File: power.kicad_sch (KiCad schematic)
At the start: 25 parts, among them J15 Screw_Terminal_01x04, U4 TPS5604, U5 TPS5604

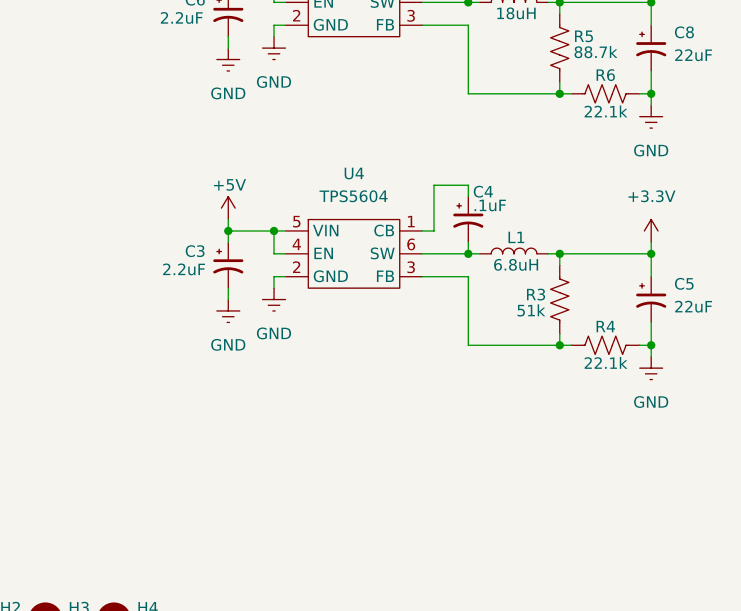
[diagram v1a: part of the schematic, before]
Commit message: mostly routed
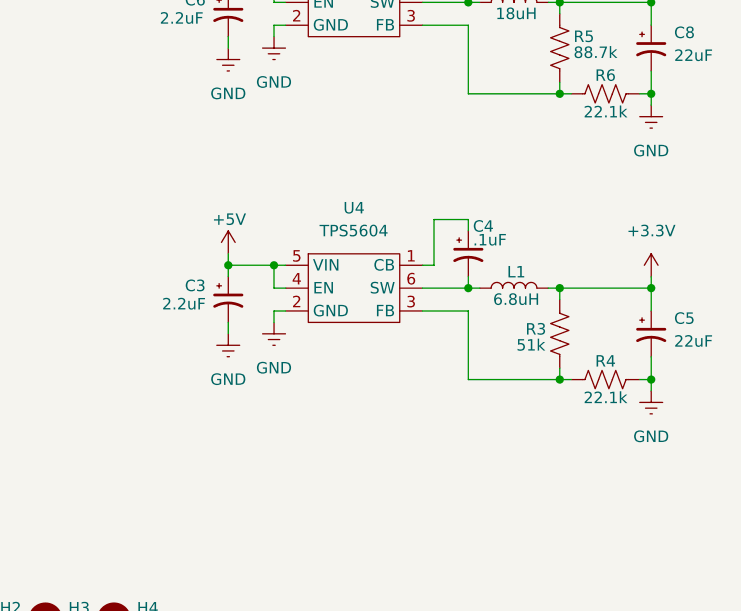
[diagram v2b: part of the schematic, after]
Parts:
- C8: footprint Capacitor_SMD:C_0805_2012Metric_Pad1.18x1.45mm_HandSolder -> Capacitor_SMD:C_0603_1608Metric_Pad1.08x0.95mm_HandSolder
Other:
- moved on the sheet: C3, C4, C5, L1, R3, R4, U4

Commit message: Rev A: release to fab (JLCPCB, 5 PCB / 2 assembled)
Board
- Outline set to exactly 160 x 100 mm; plane zones resized to match
- UART brought out on J20 (1x6 SMD, FTDI pinout) with series
  resistors R98/R99 and TVS D48
- J1 and J20 changed to SMD headers (C52016780, C41417363)
- L1/L2 moved to Sunlord SWPA4030S footprints; regulator tracks rerouted
- 41 test points added (35 top, 6 bottom), including SPI access
- Crystal case pins (Y1/Y2 pads 2, 4) tied to GND
- SW2 changed to 2-pin push button symbol
- R84-R91 changed from 2.2k to 10k to cut dissipation at 24 V
- Thermal vias in U1/U14 enlarged to 0.3 mm drill; 27 +24V vias added
  under U8-U11; solid plane connections on high-current pins
- Input/output rows and edge connectors aligned
- /inputs/_SG4 track and via moved clear of R74 pad 1

Schematic
- ERC cleared: no-connects, PWR_FLAGs, pin types, off-grid items
- Symbols moved to project library robust-io
- Test point symbols added on processor and power sheets

Rules
- Custom DRC rule for U7 pad-to-pad clearance (0.15 mm)
- Minimum through hole 0.2 mm; silk-to-edge check ignored

Fab outputs (fab/)
- make_gerbers.sh: Gerbers, drill and position export via kicad-cli
- JLC BOM with LCSC part numbers on all 50 SMD lines
- JLC placement file with per-part rotation offsets
  (cpl_rotation_offsets.json), verified in JLC placement preview
- Through-hole BOM and test point list

DRC: 4 library-mismatch warnings (J20, U1, U14, U7), 0 errors
ERC: clean
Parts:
- added TP1: +3.3V, TestPoint:TestPoint_Pad_D1.0mm, symbol Connector:TestPoint
- added TP14: ISENSE, TestPoint:TestPoint_Pad_D1.0mm, symbol Connector:TestPoint
- added TP15: ISENSE_PROT, TestPoint:TestPoint_Pad_D1.0mm, symbol Connector:TestPoint
- added TP16: AMUX0, TestPoint:TestPoint_Pad_D1.0mm, symbol Connector:TestPoint
- added TP17: IPROPIM0, TestPoint:TestPoint_Pad_D1.0mm, symbol Connector:TestPoint
- added TP18: IPROPIM1, TestPoint:TestPoint_Pad_D1.0mm, symbol Connector:TestPoint
- added TP19: DSELn, TestPoint:TestPoint_Pad_D1.0mm, symbol Connector:TestPoint
- added TP2: +5V, TestPoint:TestPoint_Pad_D1.0mm, symbol Connector:TestPoint
- added TP20: DEN0, TestPoint:TestPoint_Pad_D1.0mm, symbol Connector:TestPoint
- added TP21: DEN1, TestPoint:TestPoint_Pad_D1.0mm, symbol Connector:TestPoint
- added TP22: DEN2, TestPoint:TestPoint_Pad_D1.0mm, symbol Connector:TestPoint
- added TP23: DEN3, TestPoint:TestPoint_Pad_D1.0mm, symbol Connector:TestPoint
- added TP24: EN_M0, TestPoint:TestPoint_Pad_D1.0mm, symbol Connector:TestPoint
- added TP25: EN_M1, TestPoint:TestPoint_Pad_D1.0mm, symbol Connector:TestPoint
- added TP26: PH_M0, TestPoint:TestPoint_Pad_D1.0mm, symbol Connector:TestPoint
- added TP27: PH_M1, TestPoint:TestPoint_Pad_D1.0mm, symbol Connector:TestPoint
- added TP28: nSLEEPMn, TestPoint:TestPoint_Pad_D1.0mm, symbol Connector:TestPoint
- added TP29: FAULTMn, TestPoint:TestPoint_Pad_D1.0mm, symbol Connector:TestPoint
- added TP3: +24V, TestPoint:TestPoint_Pad_D1.0mm, symbol Connector:TestPoint
- added TP30: DRV_OUT0, TestPoint:TestPoint_Pad_D1.0mm, symbol Connector:TestPoint
- added TP31: DRV_OUT1, TestPoint:TestPoint_Pad_D1.0mm, symbol Connector:TestPoint
- added TP32: DRV_OUT2, TestPoint:TestPoint_Pad_D1.0mm, symbol Connector:TestPoint
- added TP33: DRV_OUT3, TestPoint:TestPoint_Pad_D1.0mm, symbol Connector:TestPoint
- added TP34: DRV_OUT4, TestPoint:TestPoint_Pad_D1.0mm, symbol Connector:TestPoint
- added TP35: DRV_OUT5, TestPoint:TestPoint_Pad_D1.0mm, symbol Connector:TestPoint
- added TP36: DRV_OUT6, TestPoint:TestPoint_Pad_D1.0mm, symbol Connector:TestPoint
- added TP37: DRV_OUT7, TestPoint:TestPoint_Pad_D1.0mm, symbol Connector:TestPoint
- added TP38, TP39, TP40, TP41: GND, TestPoint:TestPoint_Pad_D1.0mm, symbol Connector:TestPoint
- added TP4: SCLK0, TestPoint:TestPoint_Pad_D1.0mm, symbol Connector:TestPoint
- added TP5: MOSI0, TestPoint:TestPoint_Pad_D1.0mm, symbol Connector:TestPoint
- added TP6: MISO0, TestPoint:TestPoint_Pad_D1.0mm, symbol Connector:TestPoint
- added TP7: CS_IN0, TestPoint:TestPoint_Pad_D1.0mm, symbol Connector:TestPoint
- added TP9: INT_B0, TestPoint:TestPoint_Pad_D1.0mm, symbol Connector:TestPoint
- C44, C45: value 100uF -> 100uF 50V; footprint Capacitor_SMD:C_0805_2012Metric_Pad1.18x1.45mm_HandSolder -> Capacitor_SMD:CP_Elec_8x10
- C46: value 2.2uF -> 2.2uF 50V
- C47: value .1uF -> .1uF 50V
- D6: value SMCJ28A -> SMDJ24A
- L1: footprint Inductor_SMD:L_0805_2012Metric_Pad1.05x1.20mm_HandSolder -> Inductor_SMD:L_Sunlord_SWPA4030S
- L2: footprint Inductor_SMD:L_0805_2012Metric -> Inductor_SMD:L_Sunlord_SWPA4030S
- U4, U5: symbol rml_kicad_lib:TPS5604 -> robust-io:TPS5604
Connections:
- net +24V: now also TP3.1
- net +3.3V: now also TP1.1
- net +5V: now also TP2.1
- net GND: now also TP38.1, TP39.1, TP40.1, TP41.1
- new net AMUX0: TP16.1
- new net CS_IN0: TP7.1
- new net DEN0: TP20.1
- new net DEN1: TP21.1
- new net DEN2: TP22.1
- new net DEN3: TP23.1
- new net DRV_OUT0: TP30.1
- new net DRV_OUT1: TP31.1
- new net DRV_OUT2: TP32.1
- new net DRV_OUT3: TP33.1
- new net DRV_OUT4: TP34.1
- new net DRV_OUT5: TP35.1
- new net DRV_OUT6: TP36.1
- new net DRV_OUT7: TP37.1
- new net DSELn: TP19.1
- new net EN_M0: TP24.1
- new net EN_M1: TP25.1
- new net FAULTMn: TP29.1
- new net INT_B0: TP9.1
- new net IPROPIM0: TP17.1
- new net IPROPIM1: TP18.1
- new net ISENSE: TP14.1
- new net ISENSE_PROT: TP15.1
- new net MISO0: TP6.1
- new net MOSI0: TP5.1
- new net PH_M0: TP26.1
- new net PH_M1: TP27.1
- new net SCLK0: TP4.1
- new net nSLEEPMn: TP28.1
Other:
- moved on the sheet: C45, C46, C47
